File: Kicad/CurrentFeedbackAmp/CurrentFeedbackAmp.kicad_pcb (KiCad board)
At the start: 2 copper layers, 200 x 100 mm, 93 parts, among them J1 Vin, J10 Protecc_Sup_In1, J11 Protecc_Inf_In1, J12 Protecc_Sup_In2, J13 Vdd, J14 Vcc, J15 Masa Filtros, J16 Masa Bornera Carga, J17 Bornera Carga, J2 Test_Realim_Out, J3 Masa etapa inicial, J4 Protecc_Sup_Out, J5 Protecc_Inf_Out, J6 VccTL, J7 VddTL, J8 Test_Etapa_3_Inf, J9 Test_Etapa_3_Sup, Q1 TIP42C, Q13 BC559, Q14 BC559, Q15 BC559, Q16 BC549, Q17 BC549, Q18 BC549, Q19 BC559, Q20 BC549, Q21 BC559, Q22 BC549, Q24 BD136, Q33 BD135, Q34 TIP41C, Q35 BC559, Q36 BC549, Q37 BC549, Q38 BC549, Q39 BC549, Q40 BC559, Q41 BC559, Q42 BC559, T1 BC548, T2 BC548, U2 TL082

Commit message: Agregue reguiladores al kicad y complete las conexiones de los pines del tl082
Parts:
- added J18: Masa Reguladores, Connectors:PINTST, F.Cu at (143.8, 160.8)
- added J19: Vcc, Connectors:PINTST, F.Cu at (122.4, 147.3)
- added J20: Masa Reguladores, Connectors:PINTST, F.Cu at (125.2, 147.3)
- added J21: VccTL, Connectors:PINTST, F.Cu at (128.0, 147.5)
- added J22: Vdd, Connectors:PINTST, F.Cu at (123.6, 169.7)
- added J23: Masa Reguladores, Connectors:PINTST, F.Cu at (121.1, 169.5)
- added J24: VddTL, Connectors:PINTST, F.Cu at (126.4, 169.8)
- added J25, J26, J28, J29: VccTL, Connectors:PINTST, F.Cu at (150.0, 150.1)
- added J27: VddTL, Connectors:PINTST, F.Cu at (150.0, 150.1)
- added U1: LM7812_TO220, TO_SOT_Packages_THT:TO-220_Vertical, F.Cu at (122.4, 152.5)
- added U3: LM7912_TO220, TO_SOT_Packages_THT:TO-220_Vertical, F.Cu at (121.3, 163.2)
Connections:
- U2 pad 5: (no net) -> Net-(J29-Pad1)
- U2 pad 6: (no net) -> Net-(J28-Pad1)
- U2 pad 7: (no net) -> Net-(J25-Pad1)

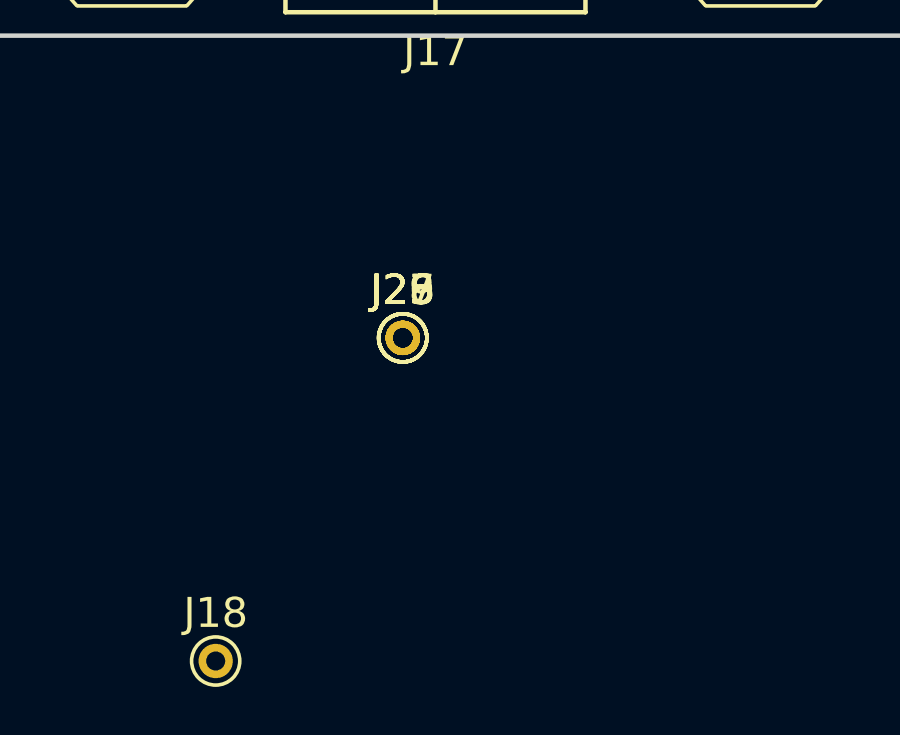
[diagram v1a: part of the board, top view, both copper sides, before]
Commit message: Conexion correcta de pines inutilizados del TL082 y la guia que explica por que
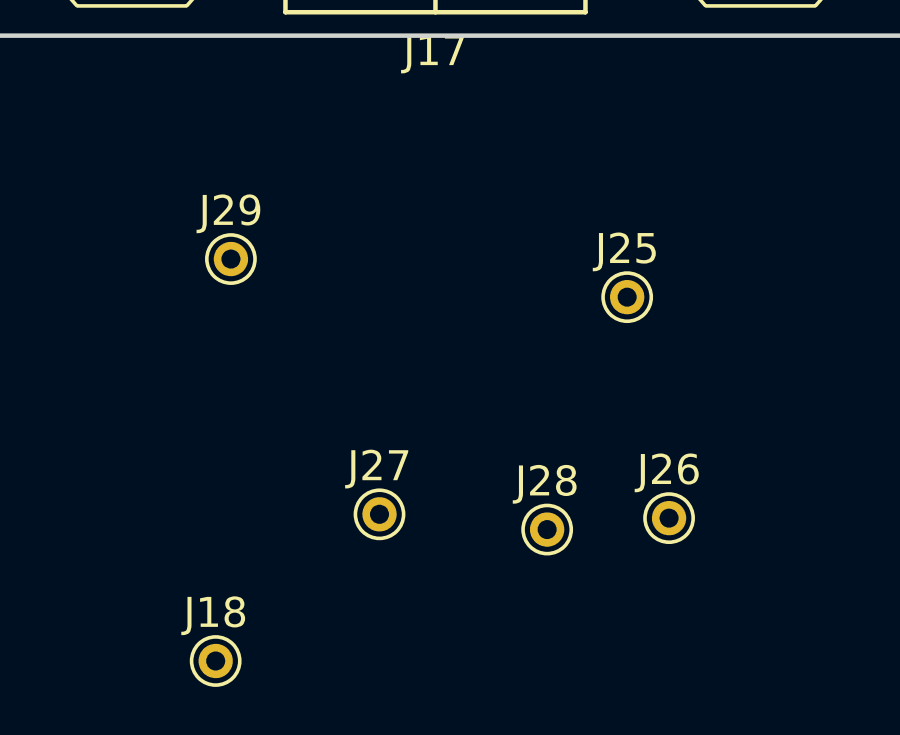
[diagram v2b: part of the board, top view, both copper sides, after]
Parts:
- J25: value VccTL -> Masa Reguladores
- moved J26 10.7 mm to (158.9, 156.1)
- moved J28 8.00 mm to (154.8, 156.5)
- moved J25 7.60 mm to (157.5, 148.7)
- moved J29 6.30 mm to (144.3, 147.4)
- moved J27 5.93 mm to (149.2, 156.0)
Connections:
- U2 pad 5: Net-(J29-Pad1) -> Net-(J25-Pad1)
- U2 pad 6: Net-(J28-Pad1) -> Net-(U2-Pad6)
- U2 pad 7: Net-(J25-Pad1) -> Net-(U2-Pad6)
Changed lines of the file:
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@@
 (kicad_pcb (version 4) (host pcbnew 4.0.7)
   (general
-    (links 152)
-    (no_connects 142)
+    (links 151)
+    (no_connects 141)
     (area 49.924999 39.924999 250.075001 140.075001)
     (thickness 1.6)
@@
     (zones 0)
     (modules 107)
-    (nets 62)
+    (nets 63)
   )
   (page A4)
@@
   (net 60 "Net-(J28-Pad1)")
   (net 61 "Net-(J29-Pad1)")
+  (net 62 "Net-(U2-Pad6)")
   (net_class Default "This is the default net class."
     (clearance 0.2)
@@
     (add_net "Net-(Rref2-Pad2)")
     (add_net "Net-(Rref3-Pad3)")
+    (add_net "Net-(U2-Pad6)")
   )
   (net_class "Corriente 2.2A" ""
@@
       (net 21 "Net-(J7-Pad1)"))
     (pad 7 smd rect (at -0.635 -3.175) (size 0.508 1.143) (layers F.Cu F.Paste F.Mask)
-      (net 57 "Net-(J25-Pad1)"))
+      (net 62 "Net-(U2-Pad6)"))
     (pad 6 smd rect (at 0.635 -3.175) (size 0.508 1.143) (layers F.Cu F.Paste F.Mask)
-      (net 60 "Net-(J28-Pad1)"))
+      (net 62 "Net-(U2-Pad6)"))
     (pad 5 smd rect (at 1.905 -3.175) (size 0.508 1.143) (layers F.Cu F.Paste F.Mask)
-      (net 61 "Net-(J29-Pad1)"))
+      (net 57 "Net-(J25-Pad1)"))
     (pad 4 smd rect (at 1.905 3.175) (size 0.508 1.143) (layers F.Cu F.Paste F.Mask)
       (net 20 "Net-(J6-Pad1)"))
@@
   )
   (module Connectors:PINTST (layer F.Cu)
-    (at 150 150.075001)
+    (at 157.48 148.717)
     (descr "module 1 pin (ou trou mecanique de percage)")
     (tags DEV)
@@
       (effects (font (size 1 1) (thickness 0.15)))
     )
-    (fp_text value VccTL (at 0 1.6) (layer F.Fab)
+    (fp_text value "Masa Reguladores" (at 0 1.6) (layer F.Fab)
       (effects (font (size 1 1) (thickness 0.15)))
     )
@@
   )
   (module Connectors:PINTST (layer F.Cu)
-    (at 150 150.075001)
+    (at 158.877 156.083)
     (descr "module 1 pin (ou trou mecanique de percage)")
     (tags DEV)
@@
   )
   (module Connectors:PINTST (layer F.Cu)
-    (at 150 150.075001)
+    (at 149.225 155.956)
     (descr "module 1 pin (ou trou mecanique de percage)")
     (tags DEV)
@@
   )
   (module Connectors:PINTST (layer F.Cu)
-    (at 150 150.075001)
+    (at 154.813 156.464)
     (descr "module 1 pin (ou trou mecanique de percage)")
     (tags DEV)
@@
   )
   (module Connectors:PINTST (layer F.Cu)
-    (at 150 150.075001)
+    (at 144.272 147.447)
     (descr "module 1 pin (ou trou mecanique de percage)")
     (tags DEV)

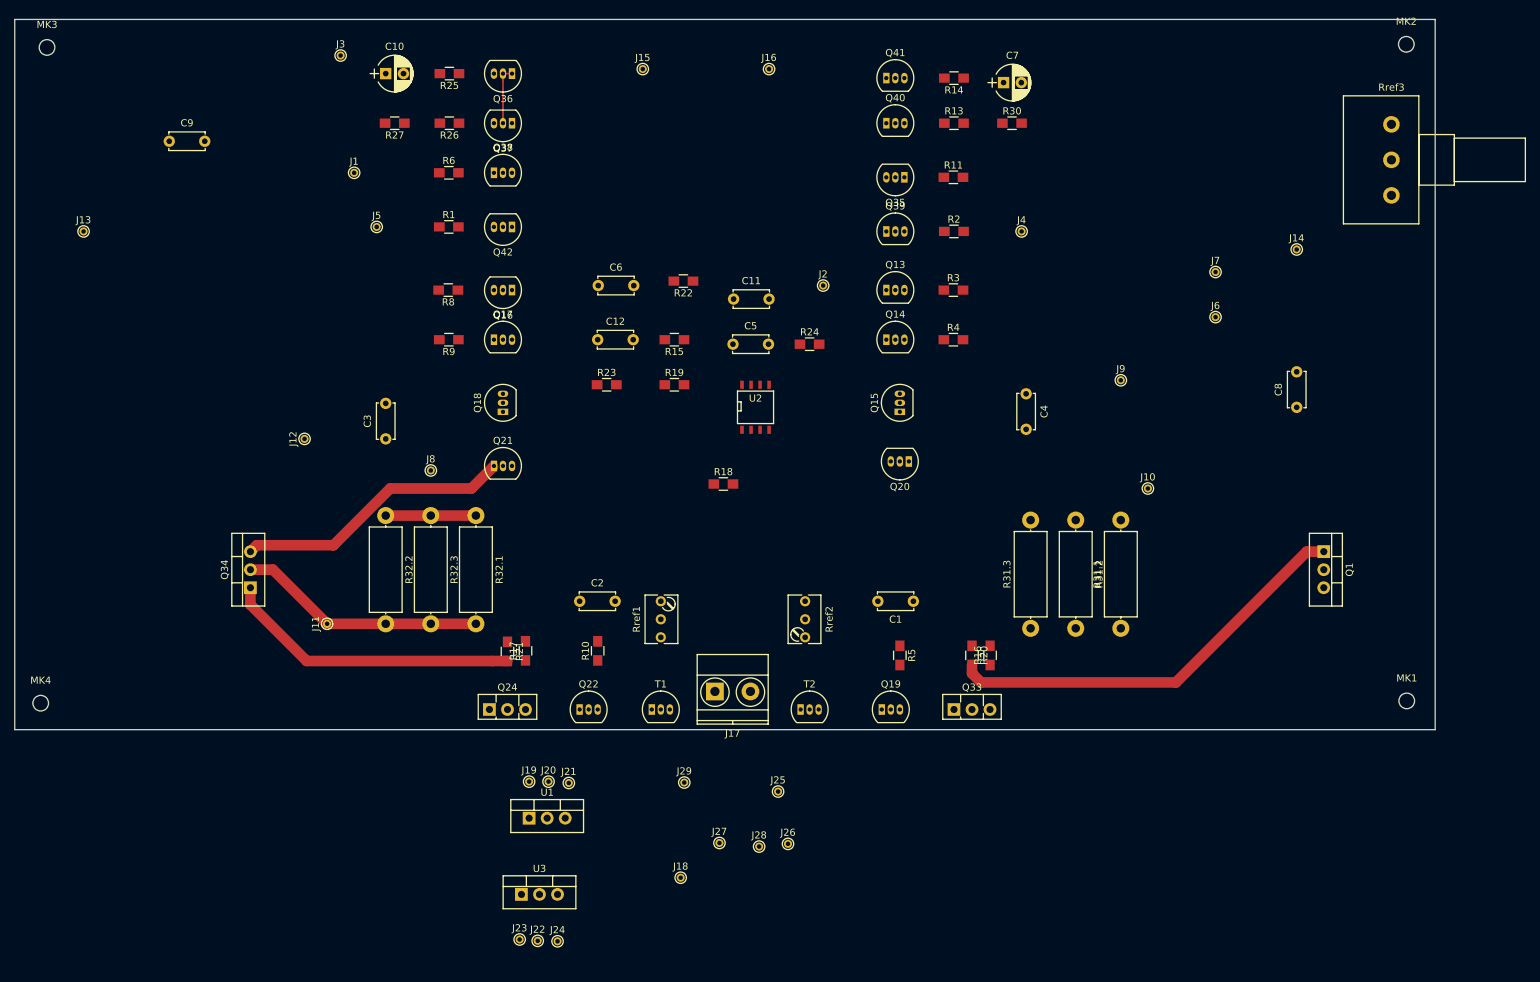
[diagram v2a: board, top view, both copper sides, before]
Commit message: Elimine algunos pins que no deberian ir porque van a ser conectados con pistas
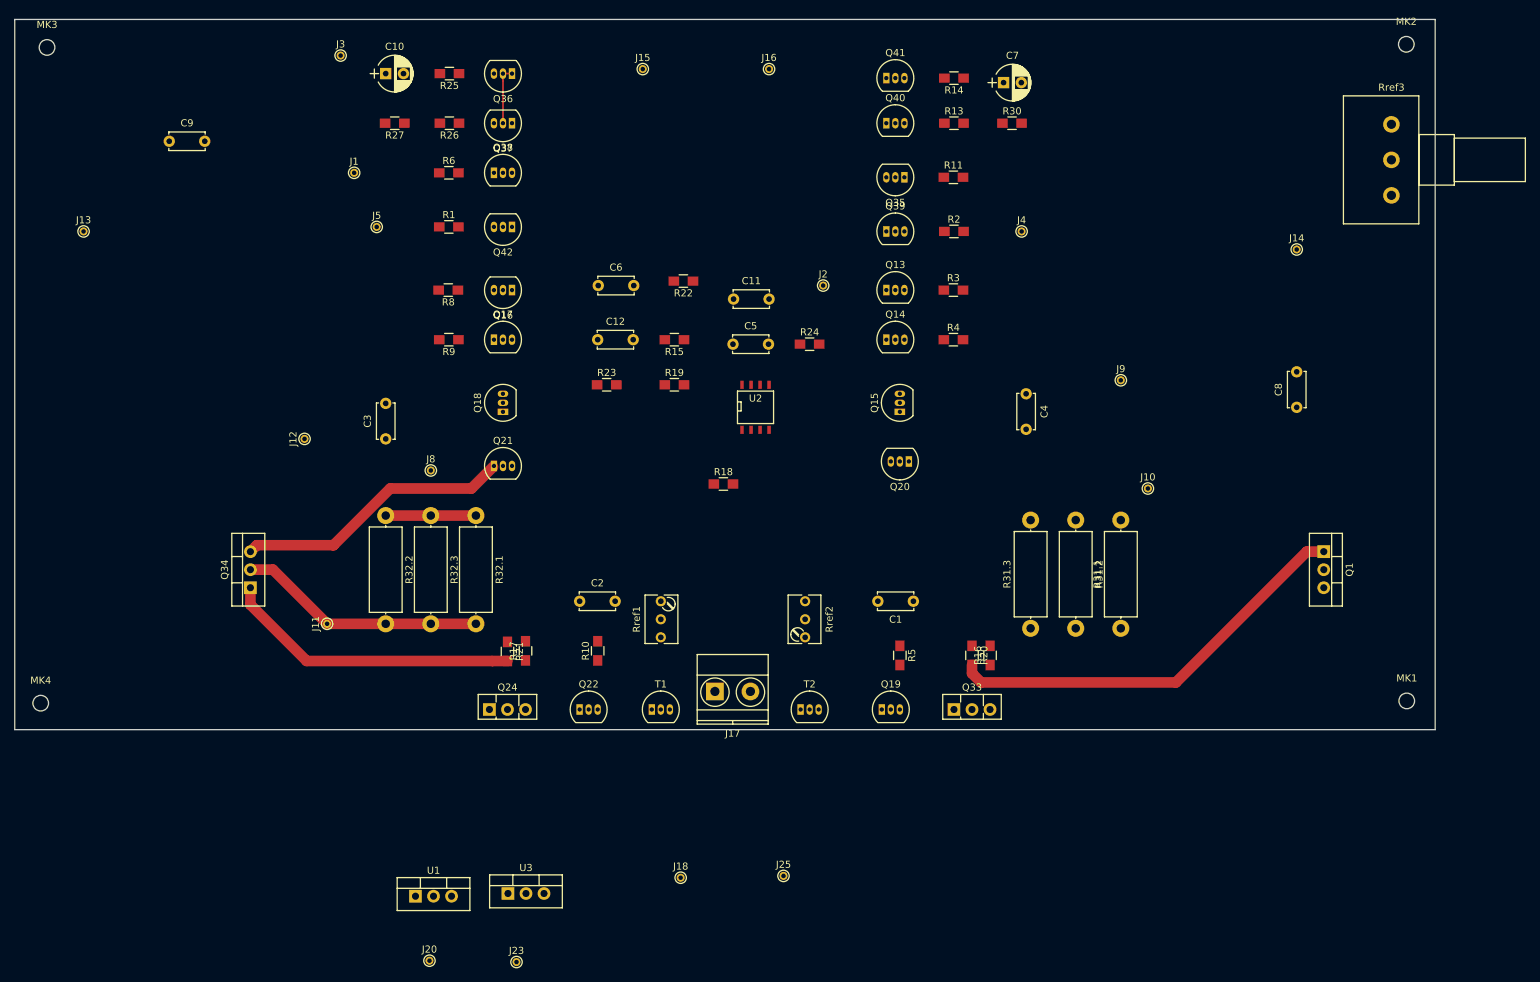
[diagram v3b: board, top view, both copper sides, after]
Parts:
- removed J19: Vcc, Connectors:PINTST
- removed J21, J26, J28, J29, J6: VccTL, Connectors:PINTST
- removed J22: Vdd, Connectors:PINTST
- removed J24, J27, J7: VddTL, Connectors:PINTST
- moved J20 30.3 mm to (108.4, 172.5)
- moved U1 19.4 mm to (106.4, 163.4)
- moved J25 11.9 mm to (158.2, 160.6)
- moved J23 3.21 mm to (120.7, 172.7)
- moved U3 1.91 mm to (119.4, 163.1)
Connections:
- C8 pad 1: Net-(C8-Pad1) -> Vcc
- C9 pad 2: Net-(C9-Pad2) -> Vdd
- J13 pad 1: Net-(C9-Pad2) -> Vdd
- J14 pad 1: Net-(C8-Pad1) -> Vcc
- Q1 pad 3: Net-(C8-Pad1) -> Vcc
- Q20 pad 1: Net-(C8-Pad1) -> Vcc
- Q21 pad 1: Net-(C9-Pad2) -> Vdd
- Q34 pad 3: Net-(C9-Pad2) -> Vdd
- R10 pad 2: Net-(C9-Pad2) -> Vdd
- R20 pad 1: Net-(C8-Pad1) -> Vcc
- R21 pad 1: Net-(C9-Pad2) -> Vdd
- R27 pad 2: Net-(C9-Pad2) -> Vdd
- R3 pad 1: Net-(C8-Pad1) -> Vcc
- R30 pad 2: Net-(C8-Pad1) -> Vcc
- R4 pad 1: Net-(C8-Pad1) -> Vcc
- R5 pad 1: Net-(C8-Pad1) -> Vcc
- R8 pad 2: Net-(C9-Pad2) -> Vdd
- R9 pad 2: Net-(C9-Pad2) -> Vdd
- U1 pad 1: Net-(J19-Pad1) -> Vcc
- U1 pad 3: Net-(J21-Pad1) -> VccTL
- U2 pad 4: Net-(J6-Pad1) -> VccTL
- U2 pad 8: Net-(J7-Pad1) -> VddTL
- U3 pad 2: Net-(J22-Pad1) -> Vdd
- U3 pad 3: Net-(J24-Pad1) -> VddTL
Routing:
- net Vdd: track 0.00 -> 39.1 mm
- net Net-(C9-Pad2): track 39.1 -> 0.00 mm

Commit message: Va la primera etapa de Rooteooooo
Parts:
- moved C8 44.0 mm to (209.6, 55.9), turned to 0 degrees
- moved R31.2 15.2 mm to (199.4, 125.7), turned to 90 degrees
- moved C1 7.62 mm to (168.9, 121.9), turned to 0 degrees
- moved Rref1 6.84 mm to (138.4, 128.3), turned to 180 degrees
- moved C2 5.08 mm to (134.6, 121.9), turned to 180 degrees
- moved Rref2 2.84 mm to (158.8, 128.3), turned to 180 degrees
- moved Q17 1.91 mm to (119.4, 85.1), turned to 180 degrees
- moved U2 0.90 mm to (154.9, 95.2), turned to 180 degrees
- moved R3 0.84 mm to (181.6, 77.5), turned to 180 degrees
- moved R13 0.63 mm to (181.6, 54.6), turned to 180 degrees
- moved R4 0.55 mm to (181.6, 85.1), turned to 180 degrees
- moved R18 0.08 mm to (149.9, 105.4), turned to 180 degrees
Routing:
- net Vcc: track 0.00 -> 218.8 mm
- net Vdd: track 39.1 -> 215.6 mm
- net GND: track 0.00 -> 130.7 mm
- net Net-(C2-Pad2): track 0.00 -> 59.8 mm
- net Net-(C3-Pad2): track 0.00 -> 45.6 mm
- net Net-(J10-Pad1): track 0.00 -> 44.7 mm
- net Net-(Q18-Pad1): track 0.00 -> 41.6 mm
- net Net-(C1-Pad1): track 0.00 -> 40.8 mm
- net Net-(C12-Pad1): track 0.00 -> 40.7 mm
- net Net-(J5-Pad1): track 0.00 -> 39.6 mm
- net DC.servo.Output: track 0.00 -> 38.3 mm
- net DC.servo.Input: track 12.7 -> 50.1 mm
- net Net-(J4-Pad1): track 0.00 -> 36.4 mm
- net Net-(Q15-Pad1): track 0.00 -> 34.6 mm
- net Net-(C4-Pad1): track 0.00 -> 29.2 mm
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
